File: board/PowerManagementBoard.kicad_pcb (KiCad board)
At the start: 2 copper layers, 170 x 99.7 mm, 152 parts, among them IC1 ACS37010LLZATR-030B3, IC2 ACS37010LLZATR-030B3, IC3 ACS37010LLZATR-030B3, IC4 ACS37010LLZATR-030B3, IC6 ACS37010LLZATR-030B3, J1 RJ45_LED_Shielded, J10 768250002, J11 768250002, J12 768250002, J13 768250002, J14 768250002, J15 768250002, J16 768250002, J17 768250002, J18 768250002, J2 SS-73100-082, J3 SS-73100-082, J5 768250002, J6 768250002, J7 768250002, J8 768250002, J9 768250002, Q1 BSS138, Q2 IPB180N10S4-02, Q3 Si4162DY, Q4 IPB180N10S4-02, Q5 Si4162DY, Q6 Si4162DY, Q7 Si4162DY, Q8 Si4162DY, Q9 IPB180N10S4-02, U1 LT1910, U10 ACS72981LLRATR-100U3, U11 LT1910, U12 LT1910, U13 LT1910, U14 LT1910, U15 Teensy4.1_DEV-16771, U16 OKI-78SR-3.3_1.5-W36H-C, U17 OKI-78SR-5_1.5-W36H-C, U19 LT1910, U2 LM5050MK-1_NOPB, U3 LM5050MK-1_NOPB, U4 Opamp_Dual, U5 Opamp_Dual, U6 Opamp_Dual

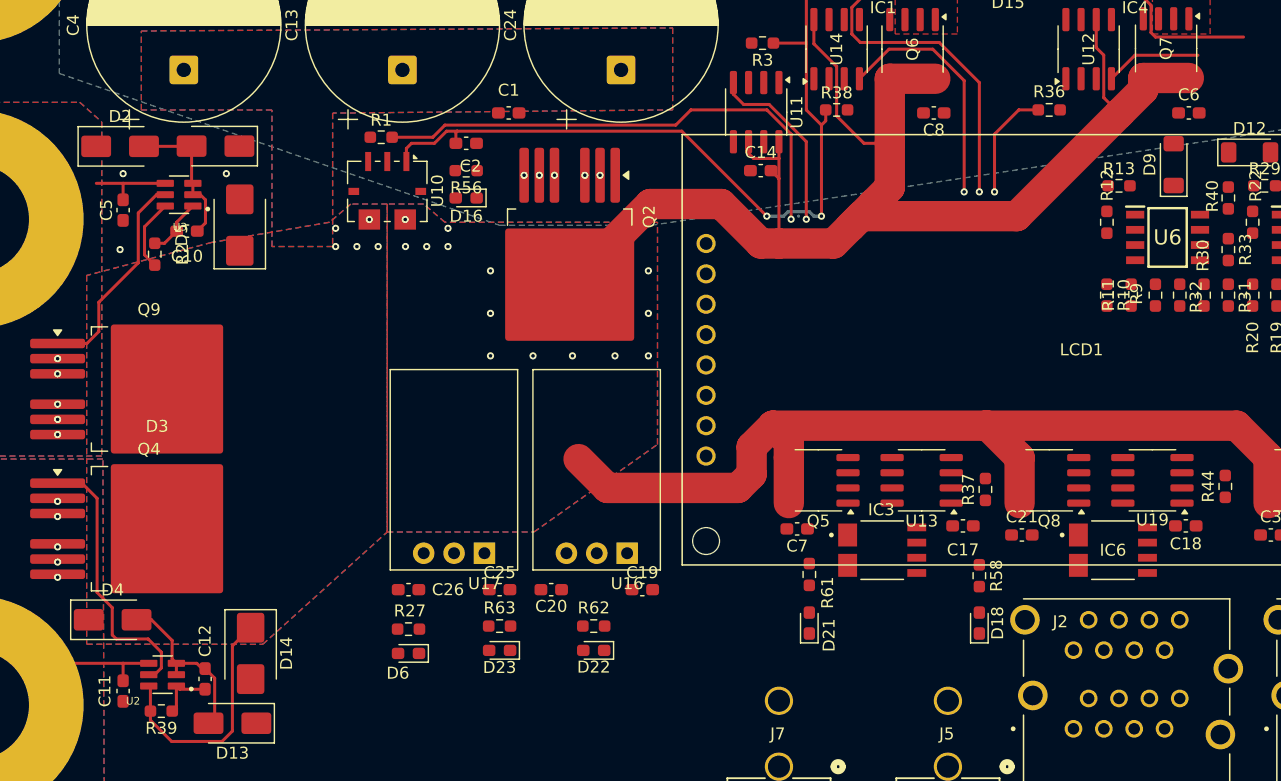
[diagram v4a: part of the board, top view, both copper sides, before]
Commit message: Some organization
+ failed artwork footprints added
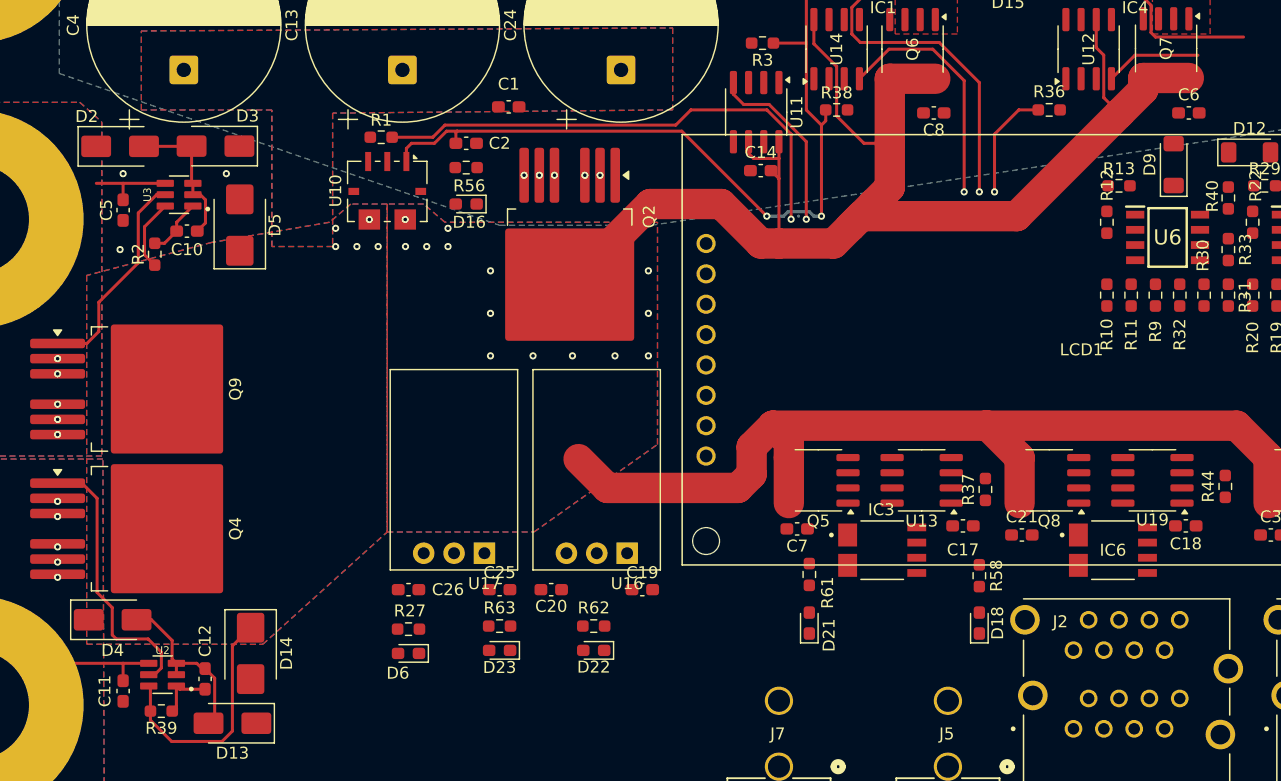
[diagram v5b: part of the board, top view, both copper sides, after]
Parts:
- moved C1 0.51 mm to (86.1, 62.5)
- moved D16 0.51 mm to (82.5, 70.6)
- moved R56 0.25 mm to (82.5, 67.6)
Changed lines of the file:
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@@
 		(tags "resistor handsolder")
 		(property "Reference" "R2"
-			(at 0 -2.315 90)
+			(at 0 1.379 90)
 			(layer "F.SilkS")
 			(effects
@@
 	(footprint "Capacitor_SMD:C_0603_1608Metric_Pad1.08x0.95mm_HandSolder"
 		(layer "F.Cu")
-		(at 86.106 62.992 180)
+		(at 86.106 62.484 180)
 		(descr "Capacitor SMD 0603 (1608 Metric), square (rectangular) end terminal, IPC-7351 nominal with elongated pad for handsoldering. (Body size source: IPC-SM-782 page 76, https://www.pcb-3d.com/wordpress/wp-content/uploads/ipc-sm-782a_amendment_1_and_2.pdf), generated with kicad-footprint-generator")
 		(tags "capacitor handsolder")
@@
 		(tags "Diode SMA (DO-214AC)")
 		(property "Reference" "D4"
-			(at 0 -2.5 0)
+			(at 0 2.559 0)
 			(layer "F.SilkS")
 			(effects
@@
 		(tags "D2PAK DDPAK TO-263 D2PAK-7 TO-263-7 SOT-427")
 		(property "Reference" "Q4"
-			(at 0 -6.65 0)
+			(at 7.227 0 90)
 			(layer "F.SilkS")
 			(effects
@@
 	(footprint "LED_SMD:LED_0603_1608Metric_Pad1.05x0.95mm_HandSolder"
 		(layer "F.Cu")
-		(at 82.55 70.104 180)
+		(at 82.55 70.612 180)
 		(descr "LED SMD 0603 (1608 Metric), square (rectangular) end terminal, IPC-7351 nominal, (Body size source: http://www.tortai-tech.com/upload/download/2011102023233369053.pdf), generated with kicad-footprint-generator")
 		(tags "LED handsolder")
 		(property "Reference" "D16"
-			(at 0 -1.524 0)
+			(at -0.254 -1.524 180)
 			(layer "F.SilkS")
 			(effects
@@
 		(at 57.15 109.982 180)
 		(property "Reference" "U2"
-			(at 2.472 -2.2064 0)
+			(at 0 2.032 0)
 			(layer "F.SilkS")
 			(effects
@@
 		(tags "resistor handsolder")
 		(property "Reference" "R32"
-			(at 0.1505 -1.367 90)
+			(at 3.302 0 90)
 			(layer "F.SilkS")
 			(effects
@@
 		(tags "capacitor handsolder")
 		(property "Reference" "C2"
-			(at 0.3575 1.905 0)
+			(at 2.794 0 0)
 			(layer "F.SilkS")
 			(effects
@@
 		(tags "Allegro PSOF-7")
 		(property "Reference" "U10"
-			(at 0 -4.2 90)
+			(at 0 4.318 90)
 			(layer "F.SilkS")
 			(effects
@@
 		(at 58.529 69.831 180)
 		(property "Reference" "U3"
-			(at -0.068 -2.7014 0)
+			(at 2.649 0 90)
 			(layer "F.SilkS")
 			(effects
@@
 	(footprint "Resistor_SMD:R_0603_1608Metric_Pad0.98x0.95mm_HandSolder"
 		(layer "F.Cu")
-		(at 82.55 67.818 180)
+		(at 82.55 67.564 180)
 		(descr "Resistor SMD 0603 (1608 Metric), square (rectangular) end terminal, IPC-7351 nominal with elongated pad for handsoldering. (Body size source: IPC-SM-782 page 72, https://www.pcb-3d.com/wordpress/wp-content/uploads/ipc-sm-782a_amendment_1_and_2.pdf), generated with kicad-footprint-generator")
 		(tags "resistor handsolder")
 		(property "Reference" "R56"
-			(at 0 -1.43 0)
+			(at -0.254 -1.524 180)
 			(layer "F.SilkS")
 			(effects
@@
 		(tags "capacitor handsolder")
 		(property "Reference" "C10"
-			(at 0 2.1 0)
+			(at 0 1.543 0)
 			(layer "F.SilkS")
 			(effects
@@
 		(tags "resistor handsolder")
 		(property "Reference" "R10"
-			(at 0 -1.43 90)
+			(at 3.302 0 90)
 			(layer "F.SilkS")
 			(effects
@@
 		(tags "Diode SMA (DO-214AC)")
 		(property "Reference" "D3"
-			(at 4.885 -23.44 0)
+			(at -2.685 2.521 0)
 			(layer "F.SilkS")
 			(effects
@@
 		(tags "Diode SMB (DO-214AA)")
 		(property "Reference" "D5"
-			(at -0.82 -4.865 90)
+			(at 0 2.939 90)
 			(layer "F.SilkS")
 			(effects
@@
 		(tags "resistor handsolder")
 		(property "Reference" "R9"
-			(at -0.112 1.5815 90)
+			(at 3.048 0 90)
 			(layer "F.SilkS")
 			(effects
@@
 		(tags "Diode SMA (DO-214AC)")
 		(property "Reference" "D2"
-			(at 0 -2.5 0)
+			(at -2.794 -2.5 0)
 			(layer "F.SilkS")
 			(effects
@@
 		(tags "resistor handsolder")
 		(property "Reference" "R11"
-			(at 0 1.905 90)
+			(at 3.302 0 90)
 			(layer "F.SilkS")
 			(effects
@@
 		(tags "D2PAK DDPAK TO-263 D2PAK-7 TO-263-7 SOT-427")
 		(property "Reference" "Q9"
-			(at 0 -6.65 0)
+			(at 7.227 0 90)
 			(layer "F.SilkS")
 			(effects

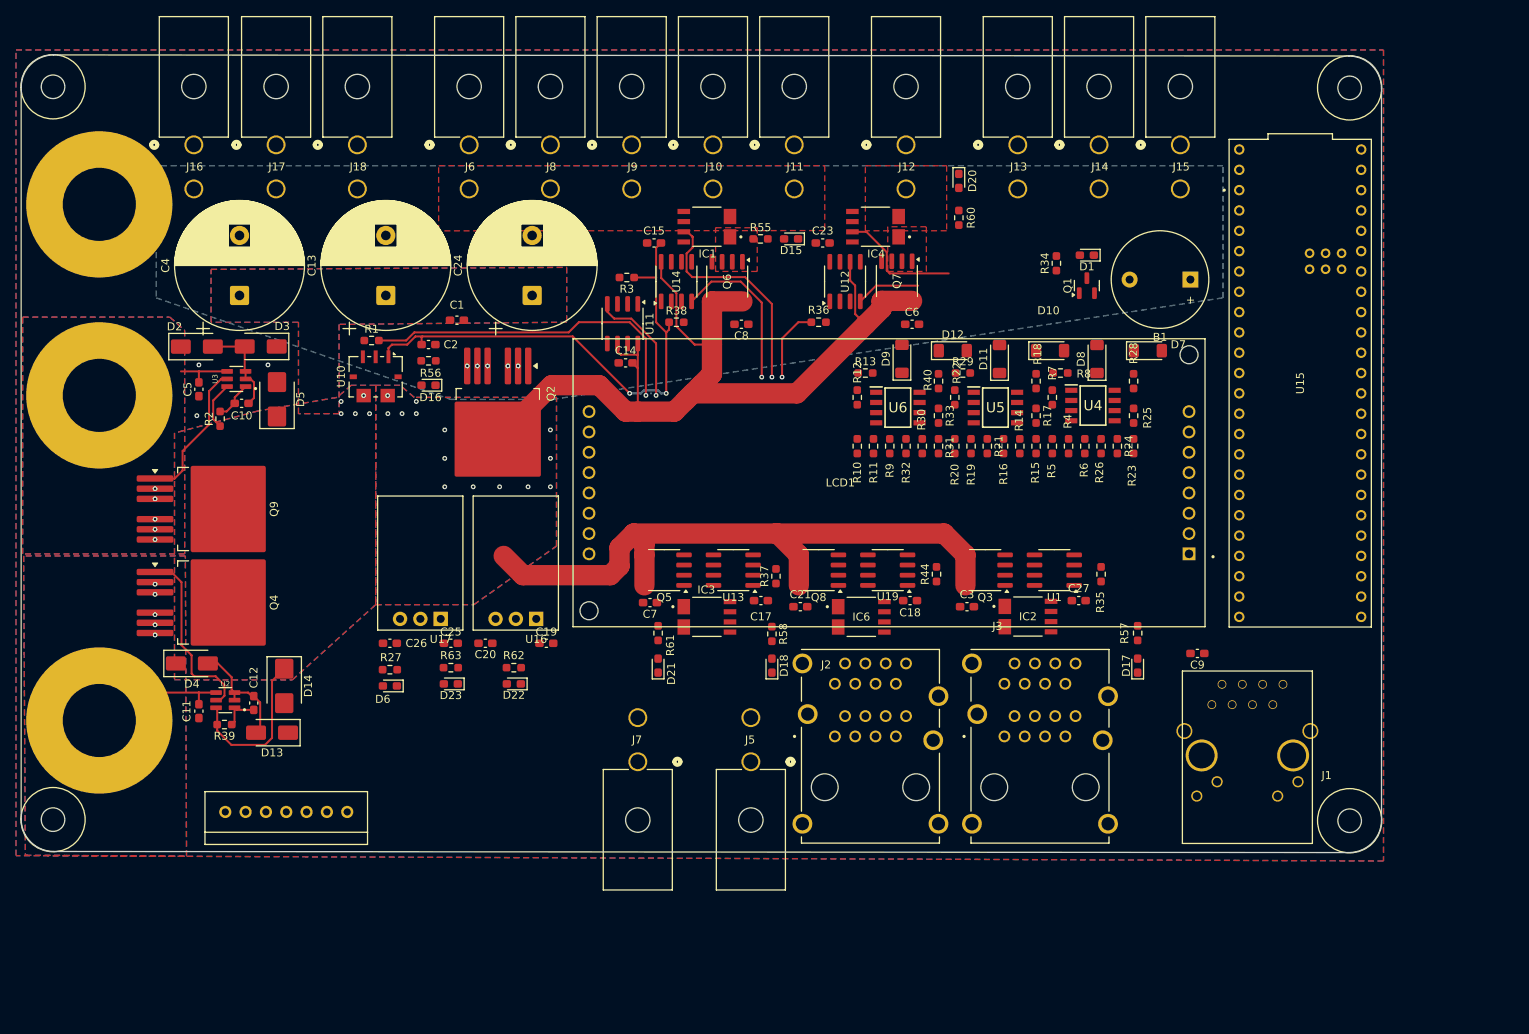
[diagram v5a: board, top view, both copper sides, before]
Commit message: layout changes for 24 volt plane
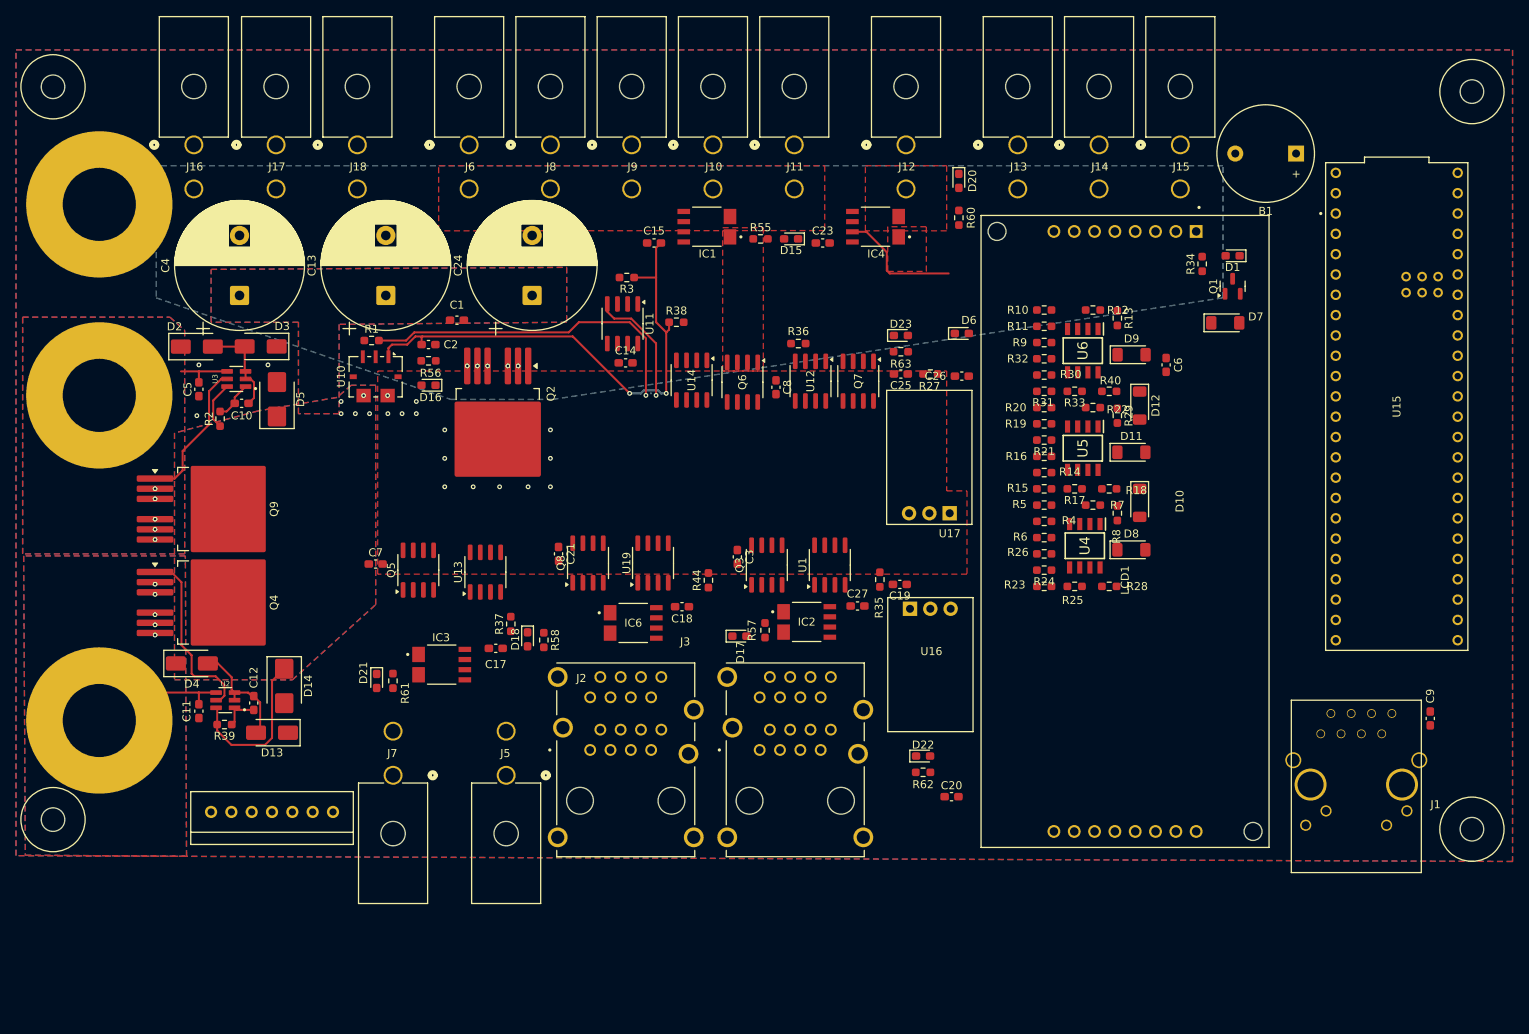
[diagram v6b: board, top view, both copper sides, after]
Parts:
- moved D6 84.0 mm to (149.2, 64.1), turned to 0 degrees
- moved C26 78.9 mm to (149.2, 69.5), turned to 0 degrees
- moved R27 77.0 mm to (145.3, 69.2), turned to 0 degrees
- moved D23 71.1 mm to (141.6, 64.4), turned to 0 degrees
- moved R63 68.7 mm to (141.6, 66.4), turned to 0 degrees
- moved C25 65.6 mm to (141.6, 69.2), turned to 180 degrees
- moved U17 65.0 mm to (147.7, 86.6)
- moved C20 61.3 mm to (147.9, 122.0), turned to 0 degrees
- moved R62 52.8 mm to (144.4, 119.0), turned to 0 degrees
- moved D22 51.9 mm to (144.4, 117.0), turned to 0 degrees
- moved D17 49.9 mm to (121.4, 102.0), turned to 0 degrees
- moved U16 46.7 mm to (142.7, 98.6), turned to 0 degrees
- moved R57 46.6 mm to (124.6, 101.2)
- moved C19 44.8 mm to (141.5, 95.5), turned to 180 degrees
- moved D21 35.2 mm to (76.1, 107.6), turned to -90 degrees
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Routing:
- net +24V: track 197.8 -> 0.00 mm
- net /Current-Sensinator/LCVout: track 27.5 -> 0.00 mm, vias 1 -> 0
- net /Switching Circuit/LC_EN: track 20.2 -> 0.00 mm, vias 1 -> 0
- net +3V3: track 73.8 -> 64.5 mm, vias 3 -> 2
- net /Switching Circuit/AUX_EN: track 8.05 -> 0.00 mm
- removed copper zone on B.Cu, net +24V
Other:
- board outline removed

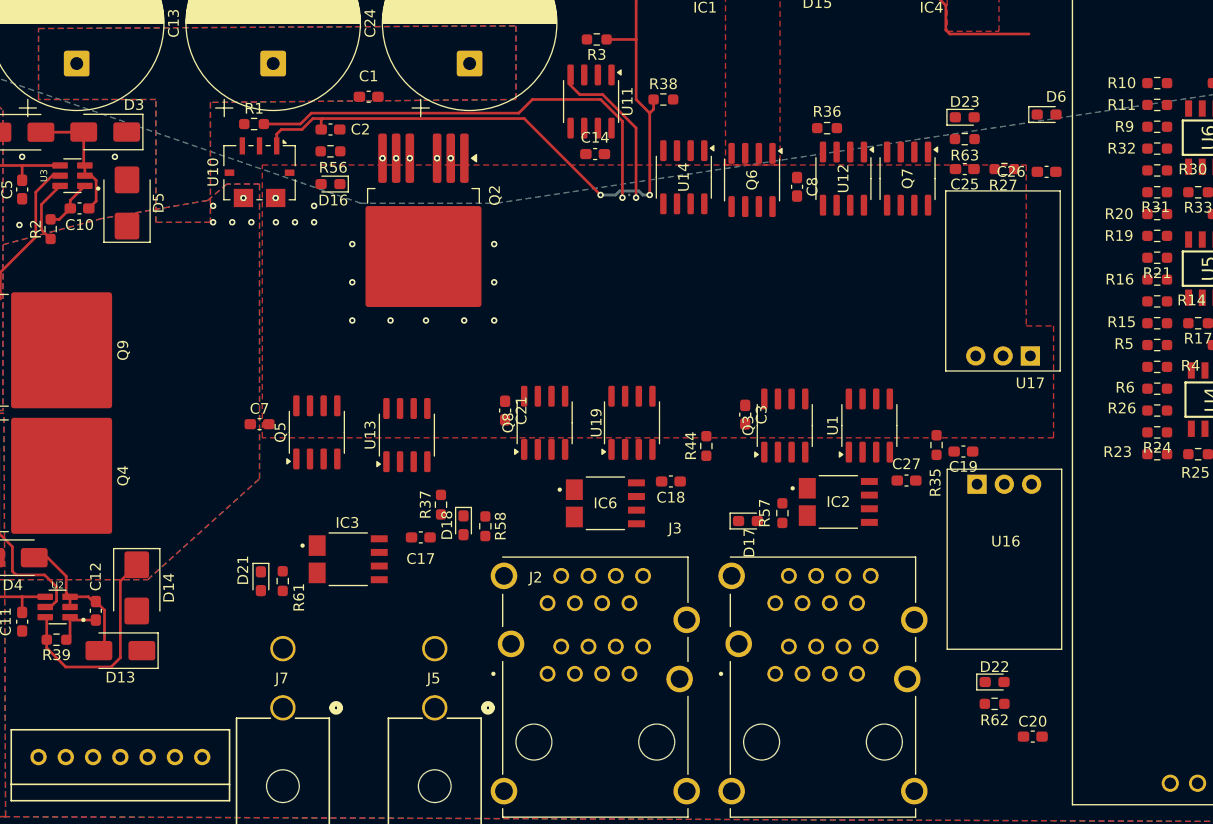
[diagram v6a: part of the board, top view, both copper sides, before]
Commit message: 24 volt plane addition
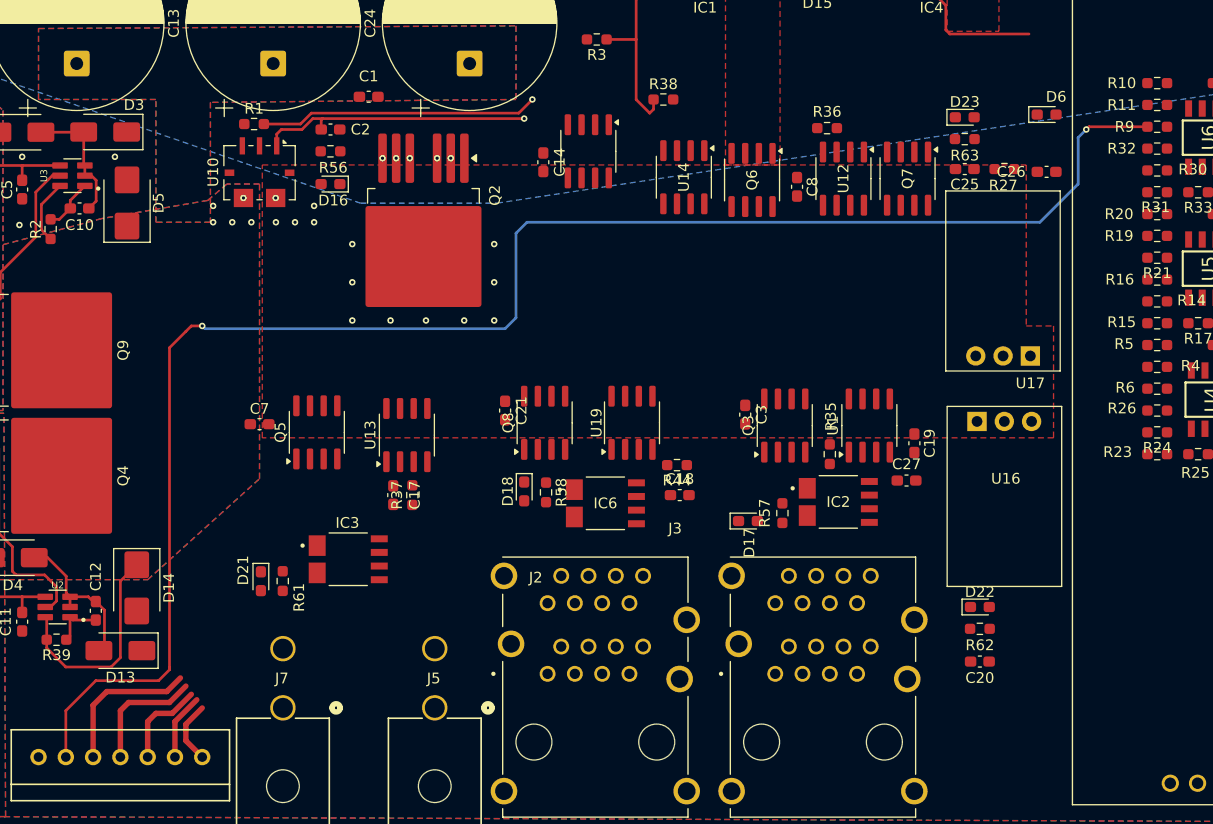
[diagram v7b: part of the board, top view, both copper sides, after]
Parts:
- moved R35 9.97 mm to (129.0, 95.8), turned to -90 degrees
- moved C20 8.55 mm to (143.0, 115.1)
- moved D22 7.12 mm to (143.0, 110.0)
- moved R62 7.12 mm to (143.0, 112.0)
- moved R58 6.47 mm to (102.6, 99.3)
- moved D18 6.47 mm to (100.6, 99.2)
- moved U16 5.85 mm to (142.7, 92.7)
- moved C14 4.89 mm to (102.4, 68.6), turned to -90 degrees
- moved C17 4.70 mm to (88.4, 99.6), turned to 90 degrees
- moved U11 4.64 mm to (106.6, 67.6)
- moved C19 4.63 mm to (136.9, 94.7), turned to -90 degrees
- moved R44 3.26 mm to (114.8, 96.8), turned to 180 degrees
- moved R37 2.81 mm to (90.2, 99.6)
- moved C18 1.51 mm to (115.1, 99.6), turned to 180 degrees
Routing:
- net Net-(Conn1-Pad6): track 0.00 -> 152.4 mm, vias 0 -> 2
- net +3V3: track 64.5 -> 41.9 mm, vias 2 -> 1
- net /Current Protection/BattVout: track 42.3 -> 25.9 mm
- net /Switching Circuit/Motor_EN: track 15.2 -> 0.00 mm, vias 1 -> 0
- net Net-(Conn1-Pad5): track 0.00 -> 14.0 mm
- net Net-(Conn1-Pad4): track 0.00 -> 11.4 mm
- net Net-(Conn1-Pad3): track 0.00 -> 8.42 mm
- net Net-(Conn1-Pad2): track 0.00 -> 6.18 mm
- net Net-(Conn1-Pad1): track 0.00 -> 5.83 mm
